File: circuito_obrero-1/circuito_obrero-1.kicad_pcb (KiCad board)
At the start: 2 copper layers, 138.6 x 79.1 mm, 48 parts, among them J1 Conn_01x03_Pin, J10 Conn_01x05, J2 Conn_01x03_Pin, J3 Conn_01x03_Pin, J4 Conn_01x03_Pin, J5 Conn_01x03_Pin, J6 Conn_01x03_Pin, J7 Conn_01x03_Pin, J8 Conn_01x03_Pin, J9 Conn_01x05, U1 74HC165, U2 74HC165, U3 74HC165

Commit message: refinando borde
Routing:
- net VCC: track 556.6 -> 558.9 mm
- added copper zone on F.Cu, net (none)
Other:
- board size 138.6 x 79.1 mm -> 136 x 75 mm

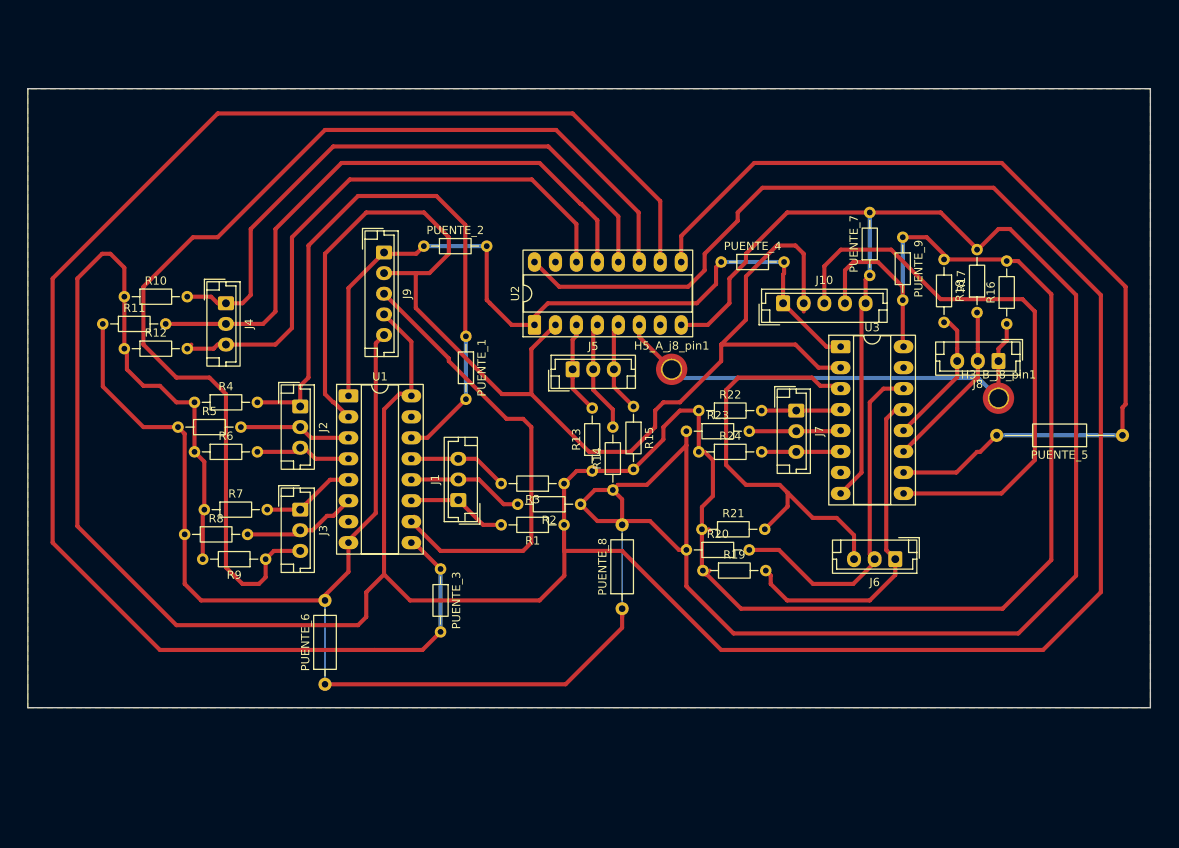
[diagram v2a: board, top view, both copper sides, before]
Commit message: redo de circuito 2 chip x 4 encoder
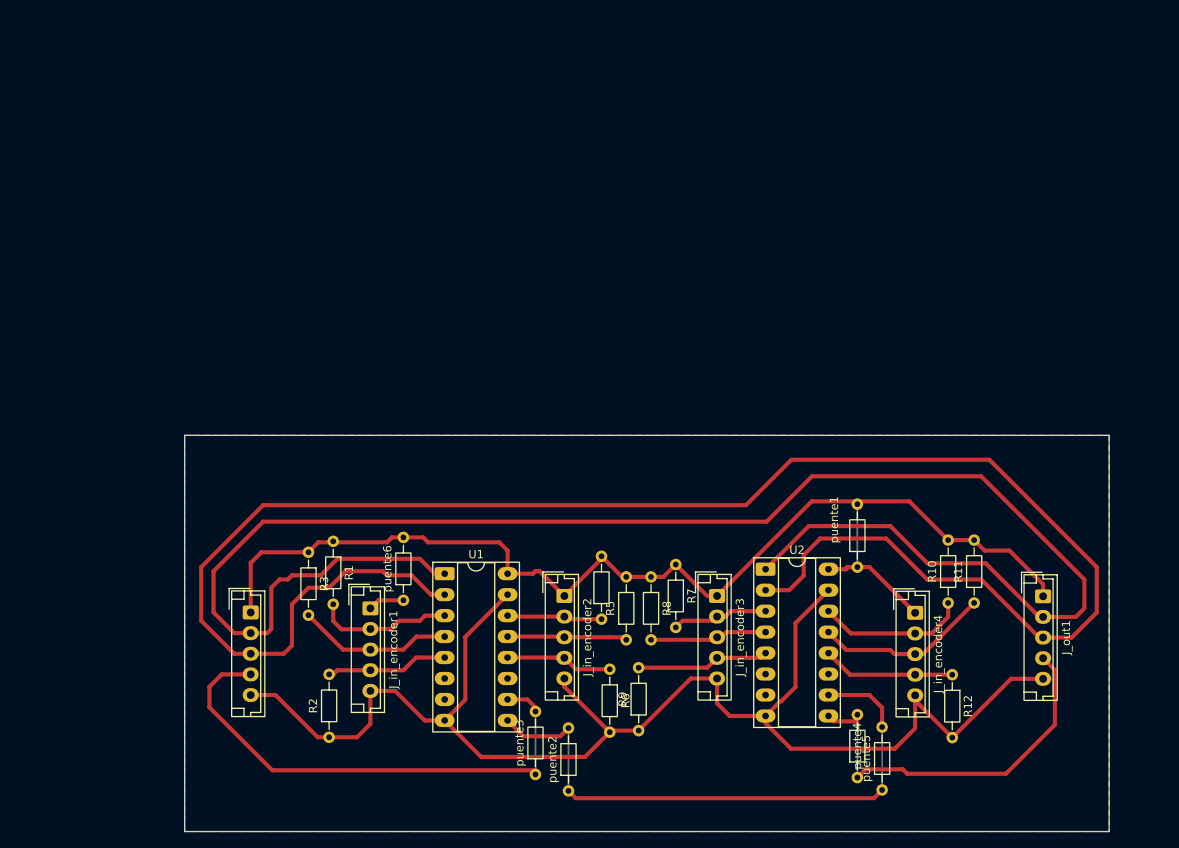
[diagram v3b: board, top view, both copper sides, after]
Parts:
- removed H3_B_j8_pin1, H5_A_j8_pin1: MountingHole_Pad, MountingHole:MountingHole_2.2mm_M2_DIN965_Pad_TopOnly
- removed J1, J2, J3, J4, J5, J6, J7, J8: Conn_01x03_Pin, Connector_JST:JST_EH_B3B-EH-A_1x03_P2.50mm_Vertical
- removed J10, J9: Conn_01x05, Connector_JST:JST_EH_B5B-EH-A_1x05_P2.50mm_Vertical
- removed PUENTE_1, PUENTE_2, PUENTE_3, PUENTE_4, PUENTE_7, PUENTE_9: 0k, Resistor_THT:R_Axial_DIN0204_L3.6mm_D1.6mm_P7.62mm_Horizontal
- removed PUENTE_5: 0k, Resistor_THT:R_Axial_DIN0207_L6.3mm_D2.5mm_P15.24mm_Horizontal
- removed PUENTE_6, PUENTE_8: 0k, Resistor_THT:R_Axial_DIN0207_L6.3mm_D2.5mm_P10.16mm_Horizontal
- removed R13, R14, R15, R16, R17, R18, R19, R20, R21, R22, R23, R24: 10k, Resistor_THT:R_Axial_DIN0204_L3.6mm_D1.6mm_P7.62mm_Horizontal
- removed U3: 74HC165, Package_DIP:CERDIP-16_W7.62mm_SideBrazed_LongPads_Socket
- added J_in1: Conn_01x05, Connector_JST:JST_EH_B5B-EH-A_1x05_P2.50mm_Vertical, F.Cu at (97.0, 97.5)
- added J_in_encoder1: Conn_01x05, Connector_JST:JST_EH_B5B-EH-A_1x05_P2.50mm_Vertical, F.Cu at (111.5, 97.0)
- added J_in_encoder2: Conn_01x05, Connector_JST:JST_EH_B5B-EH-A_1x05_P2.50mm_Vertical, F.Cu at (135.0, 95.5)
- added J_in_encoder3: Conn_01x05, Connector_JST:JST_EH_B5B-EH-A_1x05_P2.50mm_Vertical, F.Cu at (153.5, 95.5)
- added J_in_encoder4: Conn_01x05, Connector_JST:JST_EH_B5B-EH-A_1x05_P2.50mm_Vertical, F.Cu at (177.5, 97.5)
- added J_out1: Conn_01x05, Connector_JST:JST_EH_B5B-EH-A_1x05_P2.50mm_Vertical, F.Cu at (193.0, 95.5)
- added puente1: 0, Resistor_THT:R_Axial_DIN0204_L3.6mm_D1.6mm_P7.62mm_Horizontal, F.Cu at (170.5, 92.0)
- added puente2: 0, Resistor_THT:R_Axial_DIN0204_L3.6mm_D1.6mm_P7.62mm_Horizontal, F.Cu at (135.5, 119.1)
- added puente3: 0, Resistor_THT:R_Axial_DIN0204_L3.6mm_D1.6mm_P7.62mm_Horizontal, F.Cu at (131.5, 117.1)
- added puente4: 0, Resistor_THT:R_Axial_DIN0204_L3.6mm_D1.6mm_P7.62mm_Horizontal, F.Cu at (170.5, 117.5)
- added puente5: 0, Resistor_THT:R_Axial_DIN0204_L3.6mm_D1.6mm_P7.62mm_Horizontal, F.Cu at (173.5, 119.0)
- added puente6: 0, Resistor_THT:R_Axial_DIN0204_L3.6mm_D1.6mm_P7.62mm_Horizontal, F.Cu at (115.5, 96.0)
- moved R11 110.9 mm to (184.7, 96.3), turned to 90 degrees
- moved R12 107.8 mm to (182.0, 105.0), turned to -90 degrees
- moved R10 106.5 mm to (181.5, 96.3), turned to 90 degrees
- moved R5 60.1 mm to (142.5, 100.8), turned to 90 degrees
- moved R7 57.5 mm to (148.5, 91.7), turned to -90 degrees
- moved R6 56.8 mm to (140.5, 104.3), turned to -90 degrees
- moved R8 56.7 mm to (145.5, 93.2), turned to -90 degrees
- moved R4 55.9 mm to (139.5, 98.3), turned to 90 degrees
- moved R9 49.7 mm to (144.0, 111.8), turned to 90 degrees
- moved R2 41.5 mm to (106.5, 112.6), turned to 90 degrees
- moved U2 40.7 mm to (159.4, 92.2), turned to 0 degrees
- moved R3 32.1 mm to (104.0, 90.2), turned to -90 degrees
- moved R1 28.0 mm to (107.0, 88.8), turned to -90 degrees
- moved U1 24.5 mm to (120.5, 92.8)
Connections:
- R1 pad 2: Net-(J1-Pin_1) -> Net-(J_in_encoder1-Pin_2)
- R10 pad 1: VCC -> Net-(J_in_encoder4-Pin_2)
- R10 pad 2: Net-(J4-Pin_1) -> VCC
- R11 pad 1: GND -> Net-(J_in_encoder4-Pin_3)
- R11 pad 2: Net-(J4-Pin_2) -> VCC
- R12 pad 1: VCC -> Net-(J_in_encoder4-Pin_4)
- R12 pad 2: Net-(J4-Pin_3) -> GND
- R2 pad 2: Net-(J1-Pin_2) -> Net-(J_in_encoder1-Pin_4)
- R3 pad 2: Net-(J1-Pin_3) -> Net-(J_in_encoder1-Pin_3)
- R4 pad 1: VCC -> Net-(J_in_encoder2-Pin_2)
- R4 pad 2: Net-(J2-Pin_1) -> VCC
- R5 pad 1: GND -> Net-(J_in_encoder2-Pin_3)
- R5 pad 2: Net-(J2-Pin_2) -> VCC
- R6 pad 1: VCC -> Net-(J_in_encoder2-Pin_4)
- R6 pad 2: Net-(J2-Pin_3) -> GND
- R7 pad 2: Net-(J3-Pin_1) -> Net-(J_in_encoder3-Pin_2)
- R8 pad 1: GND -> VCC
- R8 pad 2: Net-(J3-Pin_2) -> Net-(J_in_encoder3-Pin_3)
- R9 pad 1: Net-(J3-Pin_3) -> GND
- R9 pad 2: VCC -> Net-(J_in_encoder3-Pin_4)
- U1 pad 11: Net-(J1-Pin_1) -> unconnected-(U1-D0-Pad11)
- U1 pad 12: Net-(J1-Pin_2) -> Net-(J_in_encoder2-Pin_4)
- U1 pad 13: Net-(J1-Pin_3) -> Net-(J_in_encoder2-Pin_3)
- U1 pad 14: Net-(J2-Pin_1) -> Net-(J_in_encoder2-Pin_2)
- U1 pad 15: unconnected-(U1-~{CE}-Pad15) -> GND
- U1 pad 3: Net-(J2-Pin_2) -> Net-(J_in_encoder1-Pin_2)
- U1 pad 4: Net-(J2-Pin_3) -> Net-(J_in_encoder1-Pin_3)
- U1 pad 5: Net-(J3-Pin_1) -> Net-(J_in_encoder1-Pin_4)
- U1 pad 6: Net-(J3-Pin_2) -> unconnected-(U1-D7-Pad6)
- U2 pad 11: Net-(J3-Pin_3) -> unconnected-(U2-D0-Pad11)
- U2 pad 12: Net-(J4-Pin_1) -> Net-(J_in_encoder4-Pin_4)
- U2 pad 13: Net-(J4-Pin_2) -> Net-(J_in_encoder4-Pin_3)
- U2 pad 14: Net-(J4-Pin_3) -> Net-(J_in_encoder4-Pin_2)
- U2 pad 15: unconnected-(U2-~{CE}-Pad15) -> GND
- U2 pad 3: Net-(J5-Pin_1) -> Net-(J_in_encoder3-Pin_2)
- U2 pad 4: Net-(J5-Pin_2) -> Net-(J_in_encoder3-Pin_3)
- U2 pad 5: Net-(J5-Pin_3) -> Net-(J_in_encoder3-Pin_4)
- U2 pad 6: Net-(J8-Pin_1) -> unconnected-(U2-D7-Pad6)
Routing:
- net VCC: track 558.9 -> 149.0 mm
- net GND: track 392.7 -> 171.9 mm
- net Net-(J3-Pin_3): track 131.3 -> 0.00 mm
- net Net-(U1-Q7): track 191.5 -> 71.5 mm
- net Net-(J_in1-Pin_2): track 94.7 -> 206.1 mm
- net Net-(J2-Pin_1): track 79.2 -> 0.00 mm
- net Net-(J4-Pin_2): track 74.2 -> 0.00 mm
- net Net-(J4-Pin_1): track 74.2 -> 0.00 mm
- net Net-(J4-Pin_3): track 69.6 -> 0.00 mm
- net Net-(J10-Pin_3): track 69.5 -> 0.00 mm
- net Net-(J_out1-Pin_4): track 113.4 -> 47.1 mm
- net Net-(J_in1-Pin_3): track 157.7 -> 221.1 mm
- net Net-(J8-Pin_1): track 57.5 -> 0.00 mm
- net Net-(J6-Pin_3): track 51.7 -> 0.00 mm
- net Net-(J6-Pin_2): track 42.4 -> 0.00 mm
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- added copper zone on F.Cu, net GND
- removed copper zone on F.Cu, net (none)
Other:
- board size 136 x 75 mm -> 112 x 48 mm

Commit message: circuito doble impresoin manual
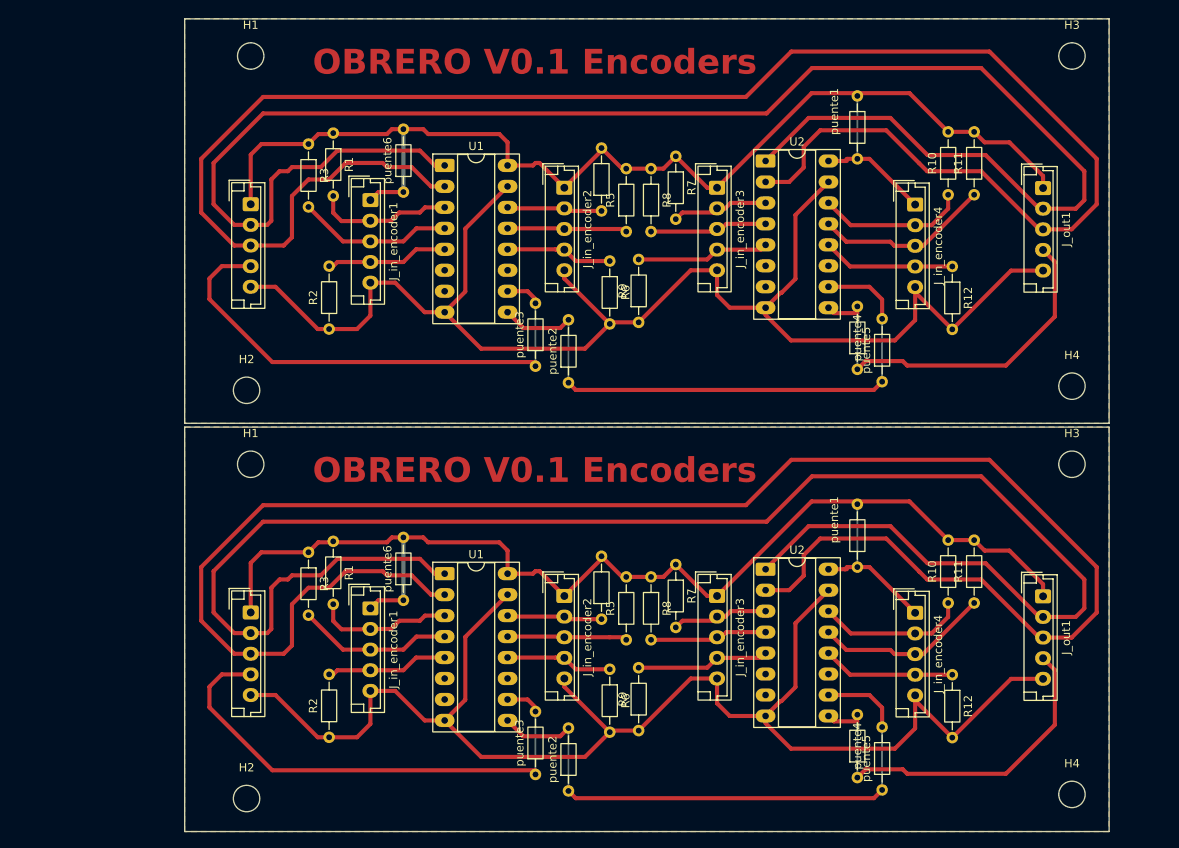
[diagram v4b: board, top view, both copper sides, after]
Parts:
- added H1: MountingHole, MountingHole:MountingHole_3.2mm_M3_DIN965, F.Cu at (97.0, 30.0)
- added H1: MountingHole, MountingHole:MountingHole_3.2mm_M3_DIN965, F.Cu at (97.0, 79.5)
- added H2: MountingHole, MountingHole:MountingHole_3.2mm_M3_DIN965, F.Cu at (96.5, 70.5)
- added H2: MountingHole, MountingHole:MountingHole_3.2mm_M3_DIN965, F.Cu at (96.5, 120.0)
- added H3: MountingHole, MountingHole:MountingHole_3.2mm_M3_DIN965, F.Cu at (196.5, 79.5)
- added H3: MountingHole, MountingHole:MountingHole_3.2mm_M3_DIN965, F.Cu at (196.5, 30.0)
- added H4: MountingHole, MountingHole:MountingHole_3.2mm_M3_DIN965, F.Cu at (196.5, 119.5)
- added H4: MountingHole, MountingHole:MountingHole_3.2mm_M3_DIN965, F.Cu at (196.5, 70.0)
- added J_in1: Conn_01x05, Connector_JST:JST_EH_B5B-EH-A_1x05_P2.50mm_Vertical, F.Cu at (97.0, 48.0)
- added J_in_encoder1: Conn_01x05, Connector_JST:JST_EH_B5B-EH-A_1x05_P2.50mm_Vertical, F.Cu at (111.5, 47.5)
- added J_in_encoder2: Conn_01x05, Connector_JST:JST_EH_B5B-EH-A_1x05_P2.50mm_Vertical, F.Cu at (135.0, 46.0)
- added J_in_encoder3: Conn_01x05, Connector_JST:JST_EH_B5B-EH-A_1x05_P2.50mm_Vertical, F.Cu at (153.5, 46.0)
- added J_in_encoder4: Conn_01x05, Connector_JST:JST_EH_B5B-EH-A_1x05_P2.50mm_Vertical, F.Cu at (177.5, 48.0)
- added J_out1: Conn_01x05, Connector_JST:JST_EH_B5B-EH-A_1x05_P2.50mm_Vertical, F.Cu at (193.0, 46.0)
- added R1: 10k, Resistor_THT:R_Axial_DIN0204_L3.6mm_D1.6mm_P7.62mm_Horizontal, F.Cu at (107.0, 39.4)
- added R10: 10k, Resistor_THT:R_Axial_DIN0204_L3.6mm_D1.6mm_P7.62mm_Horizontal, F.Cu at (181.5, 46.9)
- added R11: 10k, Resistor_THT:R_Axial_DIN0204_L3.6mm_D1.6mm_P7.62mm_Horizontal, F.Cu at (184.7, 46.9)
- added R12: 10k, Resistor_THT:R_Axial_DIN0204_L3.6mm_D1.6mm_P7.62mm_Horizontal, F.Cu at (182.0, 55.5)
- added R2: 10k, Resistor_THT:R_Axial_DIN0204_L3.6mm_D1.6mm_P7.62mm_Horizontal, F.Cu at (106.5, 63.1)
- added R3: 10k, Resistor_THT:R_Axial_DIN0204_L3.6mm_D1.6mm_P7.62mm_Horizontal, F.Cu at (104.0, 40.7)
- added R4: 10k, Resistor_THT:R_Axial_DIN0204_L3.6mm_D1.6mm_P7.62mm_Horizontal, F.Cu at (139.5, 48.8)
- added R5: 10k, Resistor_THT:R_Axial_DIN0204_L3.6mm_D1.6mm_P7.62mm_Horizontal, F.Cu at (142.5, 51.3)
- added R6: 10k, Resistor_THT:R_Axial_DIN0204_L3.6mm_D1.6mm_P7.62mm_Horizontal, F.Cu at (140.5, 54.9)
- added R7: 10k, Resistor_THT:R_Axial_DIN0204_L3.6mm_D1.6mm_P7.62mm_Horizontal, F.Cu at (148.5, 42.2)
- added R8: 10k, Resistor_THT:R_Axial_DIN0204_L3.6mm_D1.6mm_P7.62mm_Horizontal, F.Cu at (145.5, 43.7)
- added R9: 10k, Resistor_THT:R_Axial_DIN0204_L3.6mm_D1.6mm_P7.62mm_Horizontal, F.Cu at (144.0, 62.3)
- added U1: 74HC165, Package_DIP:CERDIP-16_W7.62mm_SideBrazed_LongPads_Socket, F.Cu at (120.5, 43.3)
- added U2: 74HC165, Package_DIP:CERDIP-16_W7.62mm_SideBrazed_LongPads_Socket, F.Cu at (159.4, 42.8)
- added puente1: 0, Resistor_THT:R_Axial_DIN0204_L3.6mm_D1.6mm_P7.62mm_Horizontal, F.Cu at (170.5, 42.5)
- added puente2: 0, Resistor_THT:R_Axial_DIN0204_L3.6mm_D1.6mm_P7.62mm_Horizontal, F.Cu at (135.5, 69.6)
- added puente3: 0, Resistor_THT:R_Axial_DIN0204_L3.6mm_D1.6mm_P7.62mm_Horizontal, F.Cu at (131.5, 67.6)
- added puente4: 0, Resistor_THT:R_Axial_DIN0204_L3.6mm_D1.6mm_P7.62mm_Horizontal, F.Cu at (170.5, 68.0)
- added puente5: 0, Resistor_THT:R_Axial_DIN0204_L3.6mm_D1.6mm_P7.62mm_Horizontal, F.Cu at (173.5, 69.5)
- added puente6: 0, Resistor_THT:R_Axial_DIN0204_L3.6mm_D1.6mm_P7.62mm_Horizontal, F.Cu at (115.5, 46.5)
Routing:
- net Net-(J_in1-Pin_3): track 221.1 -> 442.2 mm
- net Net-(J_in1-Pin_2): track 206.1 -> 412.3 mm
- net GND: track 171.9 -> 343.9 mm
- net VCC: track 149.0 -> 313.3 mm
- net Net-(U1-Q7): track 71.5 -> 142.9 mm
- net Net-(J_in1-Pin_4): track 62.2 -> 124.4 mm
- net Net-(J_out1-Pin_4): track 47.1 -> 94.1 mm
- net Net-(J_in_encoder4-Pin_3): track 21.3 -> 42.6 mm
- net Net-(J_in_encoder1-Pin_3): track 18.9 -> 37.8 mm
- net Net-(J_in_encoder4-Pin_2): track 18.1 -> 36.3 mm
- net Net-(J_in_encoder1-Pin_2): track 16.6 -> 33.3 mm
- net Net-(J_in_encoder3-Pin_4): track 16.1 -> 32.2 mm
- net Net-(J_in_encoder4-Pin_4): track 16.1 -> 32.2 mm
- net Net-(J_in_encoder1-Pin_4): track 14.8 -> 29.7 mm
- net Net-(J_in_encoder2-Pin_3): track 14.5 -> 29.1 mm
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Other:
- board size 112 x 48 mm -> 112 x 98.5 mm
- board text added: "OBRERO V0.1 Encoders"

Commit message: ajustes en en circuito
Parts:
- removed the H1 at (97.0, 79.5)
- removed the H2 at (96.5, 120.0)
- removed the H3 at (196.5, 79.5)
- removed the H4 at (196.5, 119.5)
- removed the J_in1 at (97.0, 97.5)
- removed the J_in_encoder1 at (111.5, 97.0)
- removed the J_in_encoder2 at (135.0, 95.5)
- removed the J_in_encoder3 at (153.5, 95.5)
- removed the J_in_encoder4 at (177.5, 97.5)
- removed the J_out1 at (193.0, 95.5)
- removed the R1 at (107.0, 88.8)
- removed the R10 at (181.5, 96.3)
- removed the R11 at (184.7, 96.3)
- removed the R12 at (182.0, 105.0)
- removed the R2 at (106.5, 112.6)
- removed the R3 at (104.0, 90.2)
- removed the R4 at (139.5, 98.3)
- removed the R5 at (142.5, 100.8)
- removed the R6 at (140.5, 104.3)
- removed the R7 at (148.5, 91.7)
- removed the R8 at (145.5, 93.2)
- removed the R9 at (144.0, 111.8)
- removed the U1 at (120.5, 92.8)
- removed the U2 at (159.4, 92.2)
- removed the puente1 at (170.5, 92.0)
- removed the puente2 at (135.5, 119.1)
- removed the puente3 at (131.5, 117.1)
- removed the puente4 at (170.5, 117.5)
- removed the puente5 at (173.5, 119.0)
- removed the puente6 at (115.5, 96.0)
- J_in1, J_in_encoder1, J_in_encoder2, J_in_encoder3, J_in_encoder4, J_out1, R1, R10, R11, R12, R2, R3, R4, R5, R6, R7, R8, R9, U1, U2, puente1, puente2, puente3, puente4, puente5, puente6: moved to B.Cu
- moved J_in1 96.0 mm to (193.0, 48.0)
- moved J_out1 96.0 mm to (97.0, 46.0)
- moved R3 82.0 mm to (186.0, 40.7)
- moved R11 79.3 mm to (105.3, 46.9)
- moved R2 77.0 mm to (183.5, 63.1)
- moved R1 76.0 mm to (183.0, 39.4)
- moved R12 74.0 mm to (108.0, 55.5)
- moved R10 73.0 mm to (108.5, 46.9)
- moved J_in_encoder1 67.0 mm to (178.5, 47.5)
- moved J_in_encoder4 65.0 mm to (112.5, 48.0)
- moved puente6 59.0 mm to (174.5, 46.5)
- moved puente5 57.0 mm to (116.5, 69.5)
- moved puente1 51.0 mm to (119.5, 42.5)
- moved puente4 51.0 mm to (119.5, 68.0)
- moved U1 49.0 mm to (169.5, 43.3), turned to 180 degrees
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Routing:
- net Net-(J_in1-Pin_3): track 442.2 -> 221.7 mm
- net Net-(J_in1-Pin_2): track 412.3 -> 203.7 mm
- net GND: track 343.9 -> 173.0 mm
- net VCC: track 313.3 -> 156.6 mm
- net Net-(U1-Q7): track 142.9 -> 71.5 mm
- net Net-(J_in1-Pin_4): track 124.4 -> 62.2 mm
- net Net-(J_out1-Pin_4): track 94.1 -> 52.1 mm
- net Net-(J_in_encoder4-Pin_3): track 42.6 -> 22.8 mm
- net Net-(J_in_encoder1-Pin_3): track 37.8 -> 18.9 mm
- net Net-(J_in_encoder4-Pin_2): track 36.3 -> 18.1 mm
- net Net-(J_in_encoder1-Pin_2): track 33.3 -> 16.6 mm
- net Net-(J_in_encoder3-Pin_4): track 32.2 -> 16.1 mm
- net Net-(J_in_encoder4-Pin_4): track 32.2 -> 16.1 mm
- net Net-(J_in_encoder1-Pin_4): track 29.7 -> 14.8 mm
- net Net-(J_in_encoder2-Pin_3): track 29.1 -> 14.5 mm
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- removed copper zone on F.Cu, net GND
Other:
- board size 112 x 98.5 mm -> 112 x 49 mm
- board text added: "OBRERO V0.2 Encoders"
- board text removed: "OBRERO V0.1 Encoders"
